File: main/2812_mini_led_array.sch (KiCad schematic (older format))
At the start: 220 parts

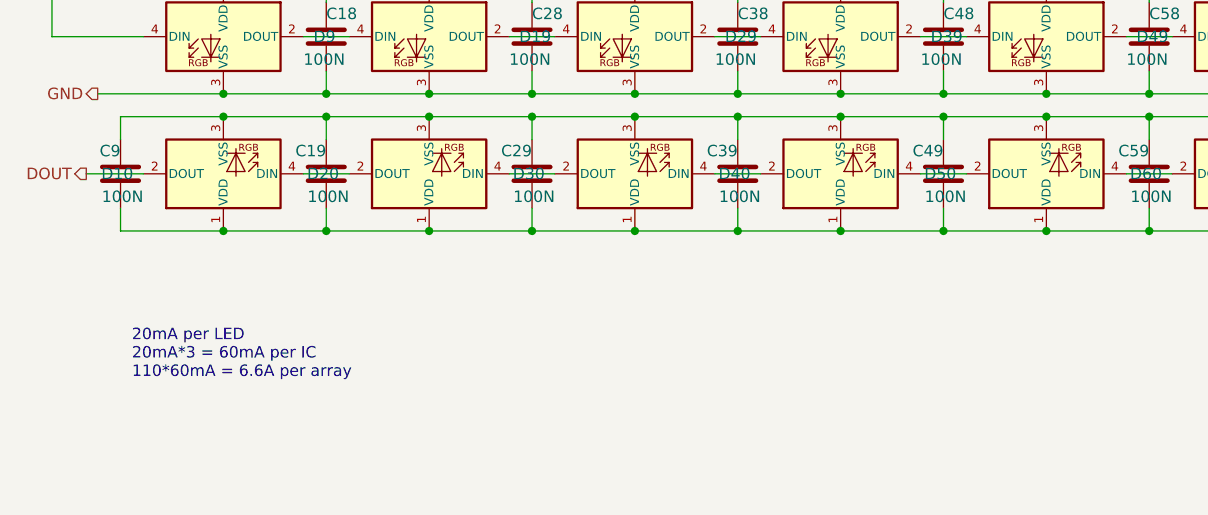
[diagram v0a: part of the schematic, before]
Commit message: added 4 more leds for minute-specific indicator
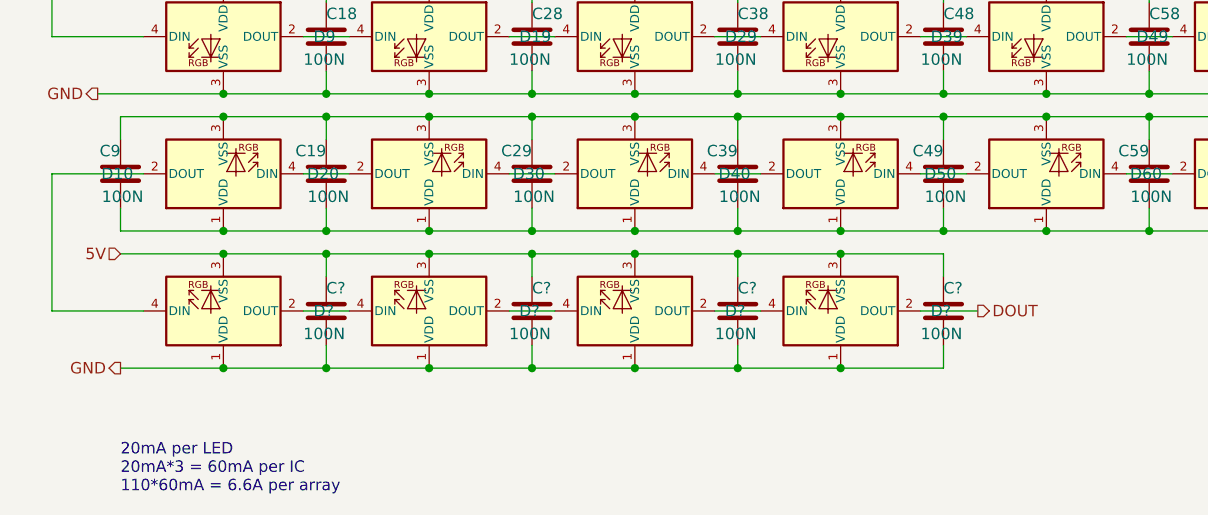
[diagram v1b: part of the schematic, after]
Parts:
- added C? (x4): 100N, Capacitor_SMD:C_0402_1005Metric, symbol Device:C
- added D? (x4): WS2812B-MINI, william_led:WS2812B_v3-MINI, symbol william_led:WS2812B-MINI
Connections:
- net 5V: now also C?.1, C?.1, C?.1, C?.1, D?.3 (VSS), D?.3 (VSS), D?.3 (VSS), D?.3 (VSS)
- net DOUT: now also D?.2 (DOUT); no longer D10.2 (DOUT)
- net GND: now also C?.2, C?.2, C?.2, C?.2, D?.1 (VDD), D?.1 (VDD), D?.1 (VDD), D?.1 (VDD)
- new net: D10.2 (DOUT), D?.4 (DIN)
- new net: D?.2 (DOUT), D?.4 (DIN) (x3)
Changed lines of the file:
@@
 Text HLabel 700  800  0    50   Input ~ 0
 DIN
-Text HLabel 650  6200 0    50   Output ~ 0
+Text HLabel 4550 6800 2    50   Output ~ 0
 DOUT
 Text HLabel 700  1050 0    50   Output ~ 0
@@
 Connection ~ 3500 6450
 Wire Wire Line
-	900  6200 650  6200
-Wire Wire Line
 	500  4400 900  4400
 Wire Wire Line
@@
 Wire Wire Line
 	500  3200 900  3200
-Text Notes 850  7100 0    50   ~ 0
+Text Notes 800  7600 0    50   ~ 0
 20mA per LED\n20mA*3 = 60mA per IC\n110*60mA = 6.6A per array
 Wire Wire Line
@@
 Wire Wire Line
 	10250 6450 10800 6450
+$Comp
+L Device:C C?
+U 1 1 5FC302C1
+P 1700 6800
+F 0 "C?" H 1700 6900 50  0000 L CNN
+F 1 "100N" H 1600 6700 50  0000 L CNN
+F 2 "Capacitor_SMD:C_0402_1005Metric" H 1738 6650 50  0001 C CNN
+F 3 "~" H 1700 6800 50  0001 C CNN
+	1    1700 6800
+	1    0    0    -1
+$EndComp
+Wire Wire Line
+	1700 6650 1700 6550
+Wire Wire Line
+	1700 6950 1700 7050
+Wire Wire Line
+	1600 6800 1800 6800
+$Comp
+L Device:C C?
+U 1 1 5FC302CE
+P 2600 6800
+F 0 "C?" H 2600 6900 50  0000 L CNN
+F 1 "100N" H 2500 6700 50  0000 L CNN
+F 2 "Capacitor_SMD:C_0402_1005Metric" H 2638 6650 50  0001 C CNN
+F 3 "~" H 2600 6800 50  0001 C CNN
+	1    2600 6800
+	1    0    0    -1
+$EndComp
+Wire Wire Line
+	2600 6650 2600 6550
+Wire Wire Line
+	2600 6950 2600 7050
+Wire Wire Line
+	2500 6800 2700 6800
+$Comp
+L Device:C C?
+U 1 1 5FC302DB
+P 3500 6800
+F 0 "C?" H 3500 6900 50  0000 L CNN
+F 1 "100N" H 3400 6700 50  0000 L CNN
+F 2 "Capacitor_SMD:C_0402_1005Metric" H 3538 6650 50  0001 C CNN
+F 3 "~" H 3500 6800 50  0001 C CNN
+	1    3500 6800
+	1    0    0    -1
+$EndComp
+Wire Wire Line
+	3500 6650 3500 6550
+Wire Wire Line
+	3500 6950 3500 7050
+Wire Wire Line
+	3400 6800 3600 6800
+$Comp
+L Device:C C?
+U 1 1 5FC302E8
+P 4400 6800
+F 0 "C?" H 4400 6900 50  0000 L CNN
+F 1 "100N" H 4300 6700 50  0000 L CNN
+F 2 "Capacitor_SMD:C_0402_1005Metric" H 4438 6650 50  0001 C CNN
+F 3 "~" H 4400 6800 50  0001 C CNN
+	1    4400 6800
+	1    0    0    -1
+$EndComp
+Wire Wire Line
+	4400 6650 4400 6550
+Wire Wire Line
+	4400 6950 4400 7050
+Connection ~ 3500 6550
+Connection ~ 3500 7050
+Connection ~ 2600 6550
+Connection ~ 2600 7050
+Connection ~ 1700 6550
+Connection ~ 1700 7050
+Wire Wire Line
+	4300 6800 4550 6800
+Wire Wire Line
+	1700 7050 1250 7050
+Wire Wire Line
+	1700 6550 1250 6550
+Wire Wire Line
+	2600 7050 2150 7050
+Wire Wire Line
+	2600 6550 2150 6550
+Wire Wire Line
+	3500 7050 3050 7050
+Wire Wire Line
+	3500 6550 3050 6550
+Wire Wire Line
+	4400 7050 3950 7050
+Wire Wire Line
+	4400 6550 3950 6550
+$Comp
+L william_led:WS2812B-MINI D?
+U 1 1 5FC30303
+P 1250 6800
+F 0 "D?" H 1644 6800 50  0000 L CNN
+F 1 "WS2812B-MINI" H 1300 6575 50  0001 L TNN
+F 2 "william_led:WS2812B_v3-MINI" H 1300 6500 50  0001 L TNN
+F 3 "https://cdn-shop.adafruit.com/datasheets/WS2812B.pdf" H 1350 6425 50  0001 L TNN
+	1    1250 6800
+	1    0    0    1
+$EndComp
+$Comp
+L william_led:WS2812B-MINI D?
+U 1 1 5FC3030D
+P 2150 6800
+F 0 "D?" H 2544 6800 50  0000 L CNN
+F 1 "WS2812B-MINI" H 2200 6575 50  0001 L TNN
+F 2 "william_led:WS2812B_v3-MINI" H 2200 6500 50  0001 L TNN
+F 3 "https://cdn-shop.adafruit.com/datasheets/WS2812B.pdf" H 2250 6425 50  0001 L TNN
+	1    2150 6800
+	1    0    0    1
+$EndComp
+$Comp
+L william_led:WS2812B-MINI D?
+U 1 1 5FC30317
+P 3050 6800
+F 0 "D?" H 3444 6800 50  0000 L CNN
+F 1 "WS2812B-MINI" H 3100 6575 50  0001 L TNN
+F 2 "william_led:WS2812B_v3-MINI" H 3100 6500 50  0001 L TNN
+F 3 "https://cdn-shop.adafruit.com/datasheets/WS2812B.pdf" H 3150 6425 50  0001 L TNN
+	1    3050 6800
+	1    0    0    1
+$EndComp
+$Comp
+L william_led:WS2812B-MINI D?
+U 1 1 5FC30321
+P 3950 6800
+F 0 "D?" H 4344 6800 50  0000 L CNN
+F 1 "WS2812B-MINI" H 4000 6575 50  0001 L TNN
+F 2 "william_led:WS2812B_v3-MINI" H 4000 6500 50  0001 L TNN
+F 3 "https://cdn-shop.adafruit.com/datasheets/WS2812B.pdf" H 4050 6425 50  0001 L TNN
+	1    3950 6800
+	1    0    0    1
+$EndComp
+Connection ~ 3950 6550
+Wire Wire Line
+	3950 6550 3500 6550
+Connection ~ 3950 7050
+Wire Wire Line
+	3950 7050 3500 7050
+Connection ~ 3050 6550
+Wire Wire Line
+	3050 6550 2600 6550
+Connection ~ 3050 7050
+Wire Wire Line
+	3050 7050 2600 7050
+Connection ~ 2150 6550
+Wire Wire Line
+	2150 6550 1700 6550
+Connection ~ 2150 7050
+Wire Wire Line
+	2150 7050 1700 7050
+Connection ~ 1250 6550
+Wire Wire Line
+	1250 6550 800  6550
+Connection ~ 1250 7050
+Wire Wire Line
+	1250 7050 800  7050
+Text HLabel 800  6550 0    50   Input ~ 0
+5V
+Text HLabel 800  7050 0    50   Output ~ 0
+GND
+Wire Wire Line
+	500  6200 500  6800
+Wire Wire Line
+	500  6800 900  6800
+Wire Wire Line
+	500  6200 900  6200
 $EndSCHEMATC

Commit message: progress and yet not.  trying for v0.2.0, but some issues: letters not aligned, switches to tall, minute leds too close to USB_C
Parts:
- D1, D10, D100, D101, D102, D103, D104, D105, D106, D107, D108, D109, D11, D110, D12, D13, D14, D15, D16, D17, D18, D19, D2, D20, D21, D22, D23, D24, D25, D26, D27, D28, D29, D3, D30, D31, D32, D33, D34, D35, D36, D37, D38, D39, D4, D40, D41, D42, D43, D44, D45, D46, D47, D48, D49, D5, D50, D51, D52, D53, D54, D55, D56, D57, D58, D59, D6, D60, D61, D62, D63, D64, D65, D66, D67, D68, D69, D7, D70, D71, D72, D73, D74, D75, D76, D77, D78, D79, D8, D80, D81, D82, D83, D84, D85, D86, D87, D88, D89, D9, D90, D91, D92, D93, D94, D95, D96, D97, D98, D99: symbol william_led:WS2812B-MINI -> main-rescue:WS2812B-MINI-william_led
- D111, D112, D113, D114: renamed from D?; symbol william_led:WS2812B-MINI -> main-rescue:WS2812B-MINI-william_led
- gave numbers to parts that had none: 4
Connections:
- net 5V: now also C101.2, C103.2, C105.2, C107.2, C109.2, C11.2, C120.2, C125.2, C126.2, C127.2, C13.2, C15.2, C17.2, C19.2, C21.2, C23.2, C25.2, C27.2, C29.2, C31.2, C33.2, C35.2, C37.2, C39.2, C41.2, C43.2, C45.2, C47.2, C49.2, C5.2, C51.2, C53.2, C55.2, C57.2, C59.2, C6.2, C61.2, C63.2, C65.2, C67.2, C69.2, C7.2, C71.2, C73.2, C75.2, C77.2, C79.2, C8.2, C81.2, C83.2, C85.2, C87.2, C89.2, C9.2, C91.2, C93.2, C95.2, C97.2, C99.2, D10.1 (VDD), D100.1 (VDD), D102.1 (VDD), D104.1 (VDD), D106.1 (VDD), D108.1 (VDD), D110.1 (VDD), D111.1 (VDD), D112.1 (VDD), D113.1 (VDD), D114.1 (VDD), D12.1 (VDD), D14.1 (VDD), D16.1 (VDD), D18.1 (VDD), D2.1 (VDD), D20.1 (VDD), D22.1 (VDD), D24.1 (VDD), D26.1 (VDD), D28.1 (VDD), D30.1 (VDD), D32.1 (VDD), D34.1 (VDD), D36.1 (VDD), D38.1 (VDD), D4.1 (VDD), D40.1 (VDD), D42.1 (VDD), D44.1 (VDD), D46.1 (VDD), D48.1 (VDD), D50.1 (VDD), D52.1 (VDD), D54.1 (VDD), D56.1 (VDD), D58.1 (VDD), D6.1 (VDD), D60.1 (VDD), D62.1 (VDD), D64.1 (VDD), D66.1 (VDD), D68.1 (VDD), D70.1 (VDD), D72.1 (VDD), D74.1 (VDD), D76.1 (VDD), D78.1 (VDD), D8.1 (VDD), D80.1 (VDD), D82.1 (VDD), D84.1 (VDD), D86.1 (VDD), D88.1 (VDD), D90.1 (VDD), D92.1 (VDD), D94.1 (VDD), D96.1 (VDD), D98.1 (VDD); no longer C101.1, C103.1, C105.1, C107.1, C109.1, C11.1, C120.1, C125.1, C126.1, C127.1, C13.1, C15.1, C17.1, C19.1, C21.1, C23.1, C25.1, C27.1, C29.1, C31.1, C33.1, C35.1, C37.1, C39.1, C41.1, C43.1, C45.1, C47.1, C49.1, C5.1, C51.1, C53.1, C55.1, C57.1, C59.1, C6.1, C61.1, C63.1, C65.1, C67.1, C69.1, C7.1, C71.1, C73.1, C75.1, C77.1, C79.1, C8.1, C81.1, C83.1, C85.1, C87.1, C89.1, C9.1, C91.1, C93.1, C95.1, C97.1, C99.1, D10.3 (VSS), D100.3 (VSS), D102.3 (VSS), D104.3 (VSS), D106.3 (VSS), D108.3 (VSS), D110.3 (VSS), D111.3 (VSS), D112.3 (VSS), D113.3 (VSS), D114.3 (VSS), D12.3 (VSS), D14.3 (VSS), D16.3 (VSS), D18.3 (VSS), D2.3 (VSS), D20.3 (VSS), D22.3 (VSS), D24.3 (VSS), D26.3 (VSS), D28.3 (VSS), D30.3 (VSS), D32.3 (VSS), D34.3 (VSS), D36.3 (VSS), D38.3 (VSS), D4.3 (VSS), D40.3 (VSS), D42.3 (VSS), D44.3 (VSS), D46.3 (VSS), D48.3 (VSS), D50.3 (VSS), D52.3 (VSS), D54.3 (VSS), D56.3 (VSS), D58.3 (VSS), D6.3 (VSS), D60.3 (VSS), D62.3 (VSS), D64.3 (VSS), D66.3 (VSS), D68.3 (VSS), D70.3 (VSS), D72.3 (VSS), D74.3 (VSS), D76.3 (VSS), D78.3 (VSS), D8.3 (VSS), D80.3 (VSS), D82.3 (VSS), D84.3 (VSS), D86.3 (VSS), D88.3 (VSS), D90.3 (VSS), D92.3 (VSS), D94.3 (VSS), D96.3 (VSS), D98.3 (VSS)
- net GND: now also C101.1, C103.1, C105.1, C107.1, C109.1, C11.1, C120.1, C125.1, C126.1, C127.1, C13.1, C15.1, C17.1, C19.1, C21.1, C23.1, C25.1, C27.1, C29.1, C31.1, C33.1, C35.1, C37.1, C39.1, C41.1, C43.1, C45.1, C47.1, C49.1, C5.1, C51.1, C53.1, C55.1, C57.1, C59.1, C6.1, C61.1, C63.1, C65.1, C67.1, C69.1, C7.1, C71.1, C73.1, C75.1, C77.1, C79.1, C8.1, C81.1, C83.1, C85.1, C87.1, C89.1, C9.1, C91.1, C93.1, C95.1, C97.1, C99.1, D10.3 (VSS), D100.3 (VSS), D102.3 (VSS), D104.3 (VSS), D106.3 (VSS), D108.3 (VSS), D110.3 (VSS), D111.3 (VSS), D112.3 (VSS), D113.3 (VSS), D114.3 (VSS), D12.3 (VSS), D14.3 (VSS), D16.3 (VSS), D18.3 (VSS), D2.3 (VSS), D20.3 (VSS), D22.3 (VSS), D24.3 (VSS), D26.3 (VSS), D28.3 (VSS), D30.3 (VSS), D32.3 (VSS), D34.3 (VSS), D36.3 (VSS), D38.3 (VSS), D4.3 (VSS), D40.3 (VSS), D42.3 (VSS), D44.3 (VSS), D46.3 (VSS), D48.3 (VSS), D50.3 (VSS), D52.3 (VSS), D54.3 (VSS), D56.3 (VSS), D58.3 (VSS), D6.3 (VSS), D60.3 (VSS), D62.3 (VSS), D64.3 (VSS), D66.3 (VSS), D68.3 (VSS), D70.3 (VSS), D72.3 (VSS), D74.3 (VSS), D76.3 (VSS), D78.3 (VSS), D8.3 (VSS), D80.3 (VSS), D82.3 (VSS), D84.3 (VSS), D86.3 (VSS), D88.3 (VSS), D90.3 (VSS), D92.3 (VSS), D94.3 (VSS), D96.3 (VSS), D98.3 (VSS); no longer C101.2, C103.2, C105.2, C107.2, C109.2, C11.2, C120.2, C125.2, C126.2, C127.2, C13.2, C15.2, C17.2, C19.2, C21.2, C23.2, C25.2, C27.2, C29.2, C31.2, C33.2, C35.2, C37.2, C39.2, C41.2, C43.2, C45.2, C47.2, C49.2, C5.2, C51.2, C53.2, C55.2, C57.2, C59.2, C6.2, C61.2, C63.2, C65.2, C67.2, C69.2, C7.2, C71.2, C73.2, C75.2, C77.2, C79.2, C8.2, C81.2, C83.2, C85.2, C87.2, C89.2, C9.2, C91.2, C93.2, C95.2, C97.2, C99.2, D10.1 (VDD), D100.1 (VDD), D102.1 (VDD), D104.1 (VDD), D106.1 (VDD), D108.1 (VDD), D110.1 (VDD), D111.1 (VDD), D112.1 (VDD), D113.1 (VDD), D114.1 (VDD), D12.1 (VDD), D14.1 (VDD), D16.1 (VDD), D18.1 (VDD), D2.1 (VDD), D20.1 (VDD), D22.1 (VDD), D24.1 (VDD), D26.1 (VDD), D28.1 (VDD), D30.1 (VDD), D32.1 (VDD), D34.1 (VDD), D36.1 (VDD), D38.1 (VDD), D4.1 (VDD), D40.1 (VDD), D42.1 (VDD), D44.1 (VDD), D46.1 (VDD), D48.1 (VDD), D50.1 (VDD), D52.1 (VDD), D54.1 (VDD), D56.1 (VDD), D58.1 (VDD), D6.1 (VDD), D60.1 (VDD), D62.1 (VDD), D64.1 (VDD), D66.1 (VDD), D68.1 (VDD), D70.1 (VDD), D72.1 (VDD), D74.1 (VDD), D76.1 (VDD), D78.1 (VDD), D8.1 (VDD), D80.1 (VDD), D82.1 (VDD), D84.1 (VDD), D86.1 (VDD), D88.1 (VDD), D90.1 (VDD), D92.1 (VDD), D94.1 (VDD), D96.1 (VDD), D98.1 (VDD)
